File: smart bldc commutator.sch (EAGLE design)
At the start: 41 parts, among them IC1 4011B, Q1 BSS123, Q2 BSS123, Q3 BSS123, Q4 BSS123, Q5 BSS123, Q6 BSS123, Q7 16MHz, U1 ATMEGA328P

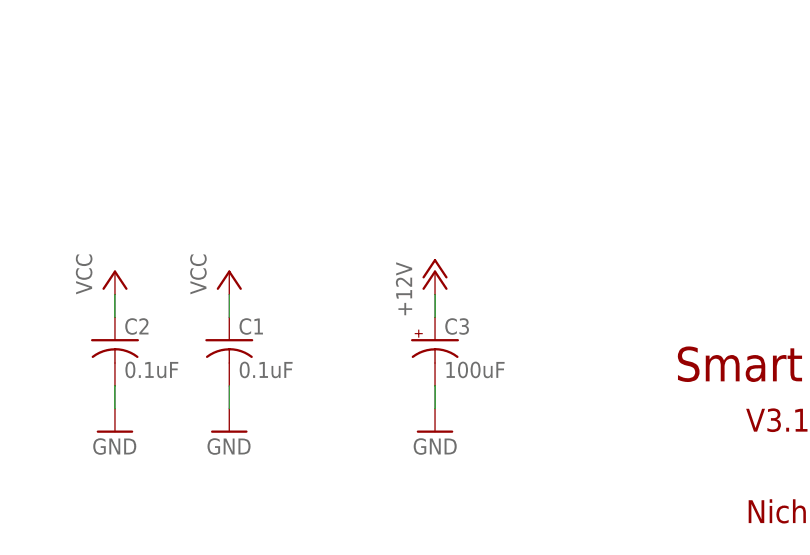
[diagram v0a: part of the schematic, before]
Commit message: Fixed +12V to VM label in schematic
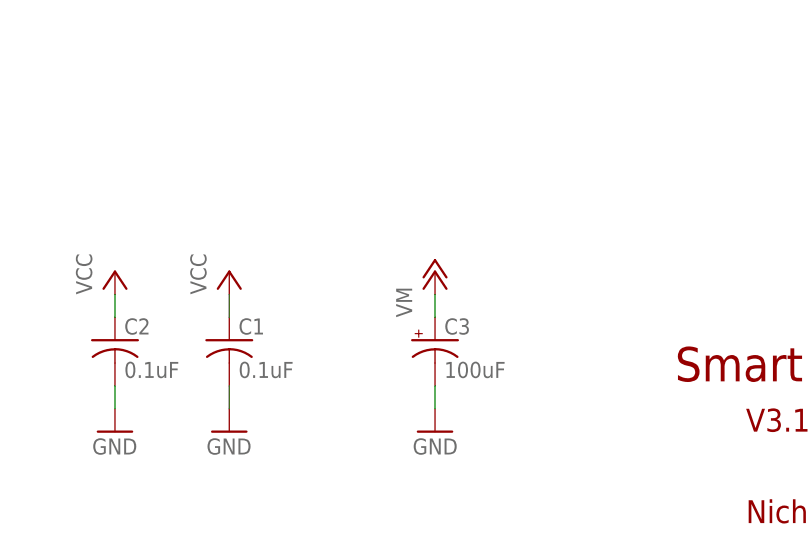
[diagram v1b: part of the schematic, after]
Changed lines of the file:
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@@
 <part name="C3" library="rcl" deviceset="CPOL-US" device="E3.5-8" value="100uF"/>
 <part name="GND5" library="supply1" deviceset="GND" device=""/>
-<part name="P+13" library="supply1" deviceset="+12V" device=""/>
+<part name="P+13" library="supply1" deviceset="+12V" device="" value="VM"/>
 <part name="Q1" library="transistor-small-signal" deviceset="BSS123" device=""/>
 <part name="GND18" library="supply1" deviceset="GND" device=""/>
